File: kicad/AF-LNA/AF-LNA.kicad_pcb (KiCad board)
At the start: 2 copper layers, 72 x 47 mm, 74 parts, among them J1 IN_SMA, J2 USB_C_Power_only, J3 LED Peak, J4 OUT_SMA, J5 LED PWR Good, Q1 2SC1815, Q2 2SC1815, SW1 SW_Short, U1 ADA4522-2, U2 ADA4522-2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

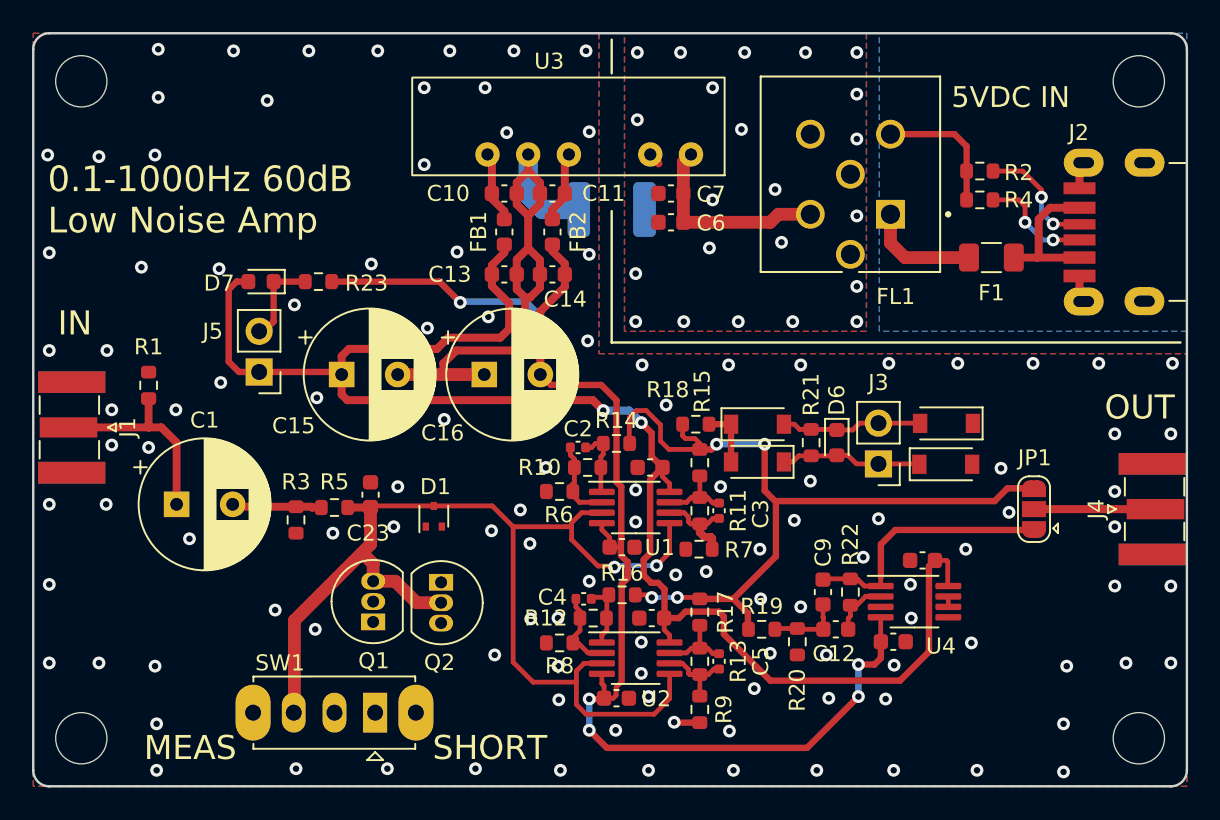
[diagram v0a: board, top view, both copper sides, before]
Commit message: Update Rev1.1
SW1位置変更、帰還抵抗GND配線をIN側SMA端子から取るように変更
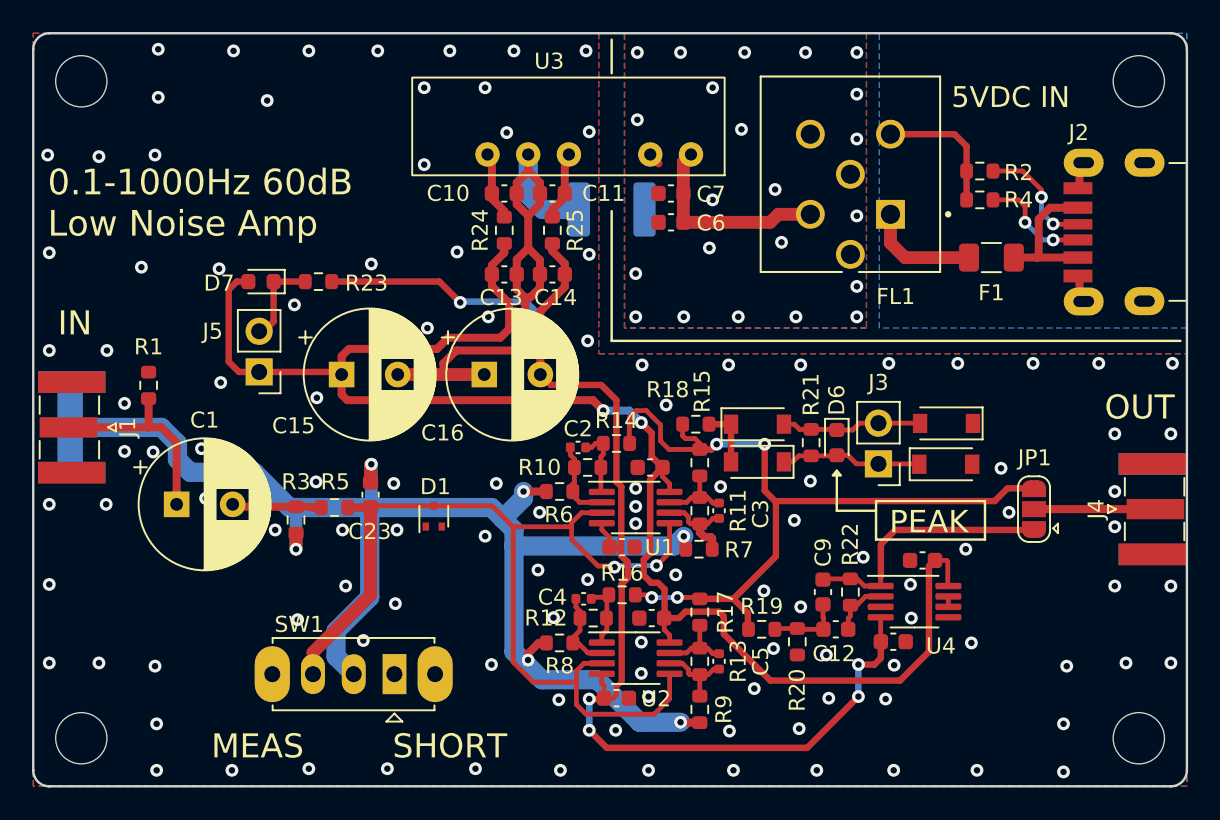
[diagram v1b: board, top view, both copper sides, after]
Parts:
- removed FB1, FB2: BLM18RK102SN1D, Inductor_SMD:L_0603_1608Metric
- removed Q1, Q2: 2SC1815, Package_TO_SOT_THT:TO-92_Inline
- added R24: 100, Resistor_SMD:R_0603_1608Metric, F.Cu at (129.4, 42.3)
- added R25: 100, Resistor_SMD:R_0603_1608Metric, F.Cu at (132.4, 42.3)
- C15, C16: value 16SEPC220MD -> 6SEPC1000MD
- moved SW1 2.75 mm to (120.0, 70.0)
- turned C23 to -90 degrees
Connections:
- C23 pad 1: Net-(C23-Pad1) -> GND2
- C23 pad 2: GNDA -> Net-(U1-Pad3)
- D1 pad 3: Net-(C23-Pad1) -> Net-(U1-Pad3)
- R3 pad 2: GNDA -> GND2
- R5 pad 2: Net-(C23-Pad1) -> Net-(U1-Pad3)
- R6 pad 2: GNDA -> GND2
- R7 pad 2: GNDA -> GND2
- R8 pad 2: GNDA -> GND2
- R9 pad 2: GNDA -> GND2
- SW1 pad 2: GNDA -> GND2
- SW1 pad 3: Net-(C23-Pad1) -> Net-(U1-Pad3)
- U1 pad 3: Net-(C23-Pad1) -> Net-(U1-Pad3)
- U1 pad 5: Net-(C23-Pad1) -> Net-(U1-Pad3)
- U2 pad 3: Net-(C23-Pad1) -> Net-(U1-Pad3)
- U2 pad 5: Net-(C23-Pad1) -> Net-(U1-Pad3)
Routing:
- net GND2: track 0.00 -> 88.4 mm, vias 0 -> 6
- net Net-(C23-Pad1): track 72.9 -> 0.00 mm, vias 2 -> 0
- net Net-(U1-Pad3): track 0.00 -> 63.2 mm, vias 0 -> 2
- net GNDA: track 39.0 -> 37.4 mm, vias 121 -> 120
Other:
- board text added: "2022-07-04 Rev1.1 https://github.com/kingyoPiyo"
- board text added: "PEAK"
- board text removed: "2022-06-05 Rev1.0 kingyonull"
